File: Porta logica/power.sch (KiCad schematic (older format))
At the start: 7 parts, among them P3 Batteria, P4 Alimentatore, U5 LM7805

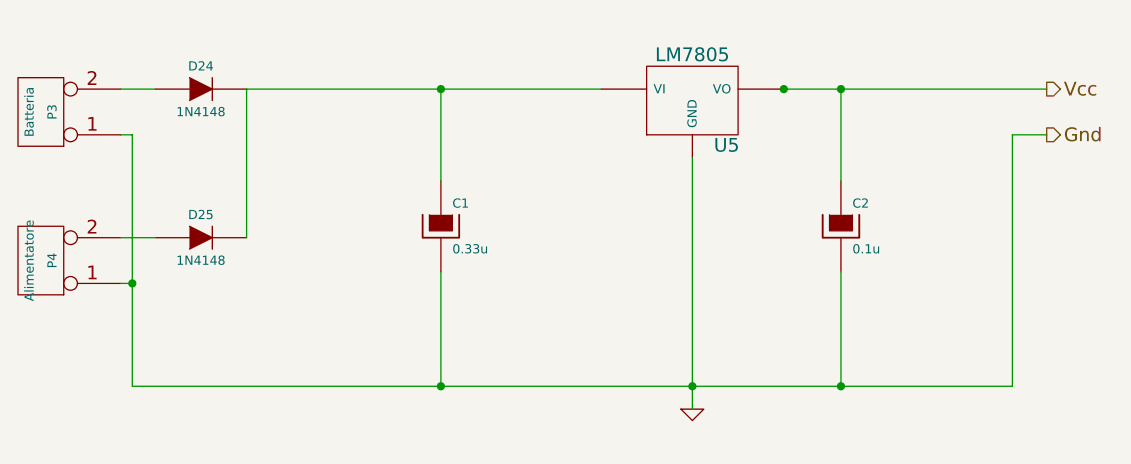
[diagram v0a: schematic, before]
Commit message: correzione bug, migliorie grafiche
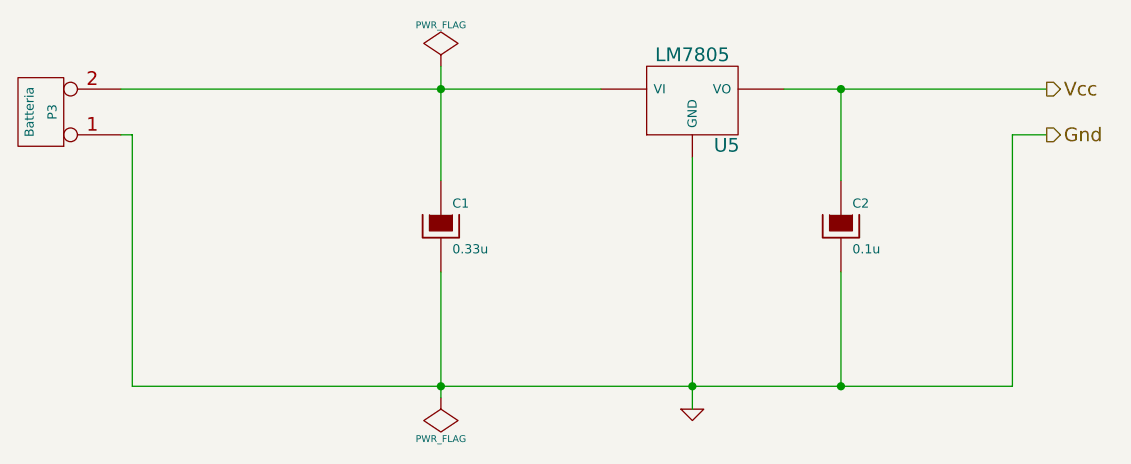
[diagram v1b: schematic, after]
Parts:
- removed D24, D25: 1N4148, ~, symbol DIODE
- removed P4: Alimentatore, symbol CONN_2
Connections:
- net at P3.2 (PM): now also C1.1, U5.VI
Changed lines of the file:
@@
 Connection ~ 6300 3500
 Wire Wire Line
-	4550 2600 4550 2200
+	4550 2100 4550 2600
 Connection ~ 4550 2200
 Wire Wire Line
-	4550 3000 4550 3500
+	4550 3000 4550 3550
 Connection ~ 4550 3500
 $Comp
-L GND #PWR020
+L GND #PWR016
 U 1 1 555B893B
 P 5650 3600
-F 0 "#PWR020" H 5650 3600 30  0001 C CNN
+F 0 "#PWR016" H 5650 3600 30  0001 C CNN
 F 1 "GND" H 5650 3530 30  0001 C CNN
 F 2 "" H 5650 3600 60  0000 C CNN
@@
 	1    0    0    -1
 $EndComp
-$Comp
-L CONN_2 P4
-U 1 1 555B8B69
-P 2800 2950
-F 0 "P4" V 2750 2950 40  0000 C CNN
-F 1 "Alimentatore" V 2850 2950 40  0000 C CNN
-F 2 "" H 2800 2950 60  0000 C CNN
-F 3 "" H 2800 2950 60  0000 C CNN
-	1    2800 2950
-	-1   0    0    1
-$EndComp
-$Comp
-L DIODE D24
-U 1 1 555B8B78
-P 3500 2200
-F 0 "D24" H 3500 2300 40  0000 C CNN
-F 1 "1N4148" H 3500 2100 40  0000 C CNN
-F 2 "~" H 3500 2200 60  0000 C CNN
-F 3 "~" H 3500 2200 60  0000 C CNN
-	1    3500 2200
-	1    0    0    -1
-$EndComp
-$Comp
-L DIODE D25
-U 1 1 555B8B85
-P 3500 2850
-F 0 "D25" H 3500 2950 40  0000 C CNN
-F 1 "1N4148" H 3500 2750 40  0000 C CNN
-F 2 "~" H 3500 2850 60  0000 C CNN
-F 3 "~" H 3500 2850 60  0000 C CNN
-	1    3500 2850
-	1    0    0    -1
-$EndComp
 Wire Wire Line
-	3150 2850 3300 2850
-Wire Wire Line
-	3150 2200 3300 2200
-Wire Wire Line
-	3700 2200 3700 2850
-Wire Wire Line
-	3700 2200 5250 2200
+	3150 2200 5250 2200
 Wire Wire Line
 	3150 2400 3200 2400
@@
 	3200 2400 3200 3500
 Wire Wire Line
-	3200 3050 3150 3050
-Connection ~ 3200 3050
-Wire Wire Line
 	6050 2200 7200 2200
 Wire Wire Line
 	6300 2600 6300 2200
 Connection ~ 6300 2200
-Connection ~ 6050 2200
+$Comp
+L PWR_FLAG #FLG017
+U 1 1 555CE9F0
+P 4550 2100
+F 0 "#FLG017" H 4550 2195 30  0001 C CNN
+F 1 "PWR_FLAG" H 4550 2280 30  0000 C CNN
+F 2 "" H 4550 2100 60  0000 C CNN
+F 3 "" H 4550 2100 60  0000 C CNN
+	1    4550 2100
+	1    0    0    -1
+$EndComp
+$Comp
+L PWR_FLAG #FLG018
+U 1 1 555D38D4
+P 4550 3550
+F 0 "#FLG018" H 4550 3645 30  0001 C CNN
+F 1 "PWR_FLAG" H 4550 3730 30  0000 C CNN
+F 2 "" H 4550 3550 60  0000 C CNN
+F 3 "" H 4550 3550 60  0000 C CNN
+	1    4550 3550
+	-1   0    0    1
+$EndComp
 $EndSCHEMATC
